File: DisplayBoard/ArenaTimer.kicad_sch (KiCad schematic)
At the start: 42 parts, among them J1 Blue ready-up, J10 Red ready-up, J12 Screw_Terminal_01x03, J13 WAGO, J14 WAGO, J15 Conn_01x15_Socket, J16 Conn_01x15_Socket, J2 Conn_01x02_Socket, J3 Conn_01x02_Pin, J4 GND, J5 5V, J6 GND, J7 5V, J8 PJ-082BH, J9 Conn_01x06_Pin, K1 G5V-2_Split, Q1 BSS214NW

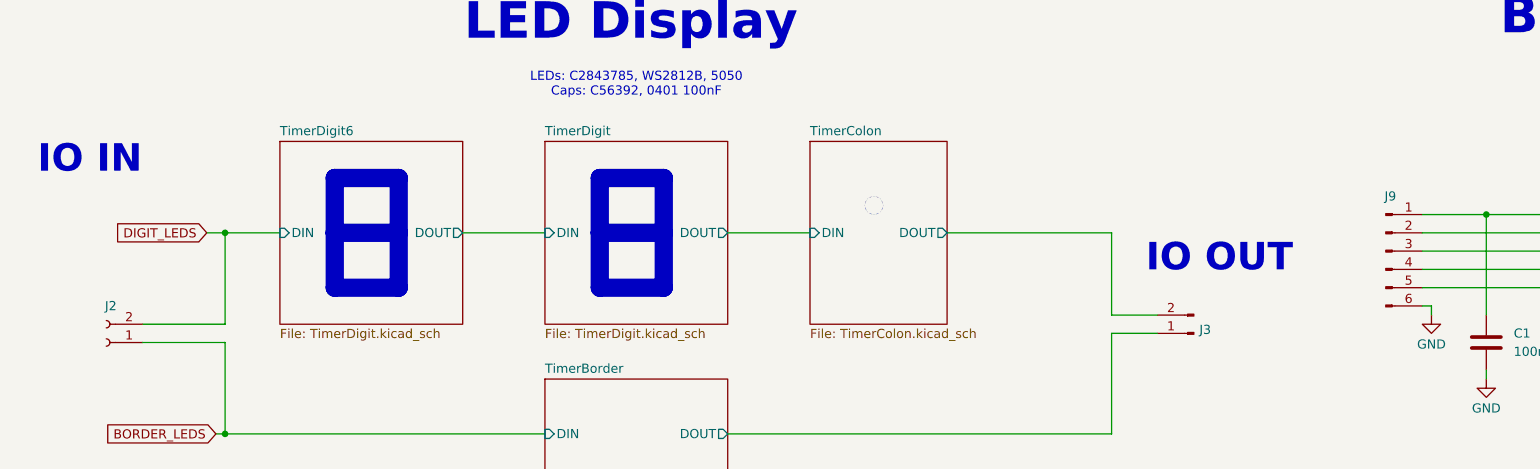
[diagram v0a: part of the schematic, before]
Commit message: flip BOUT/DOUT which is techncially flipped, but consistent with legacy HW.
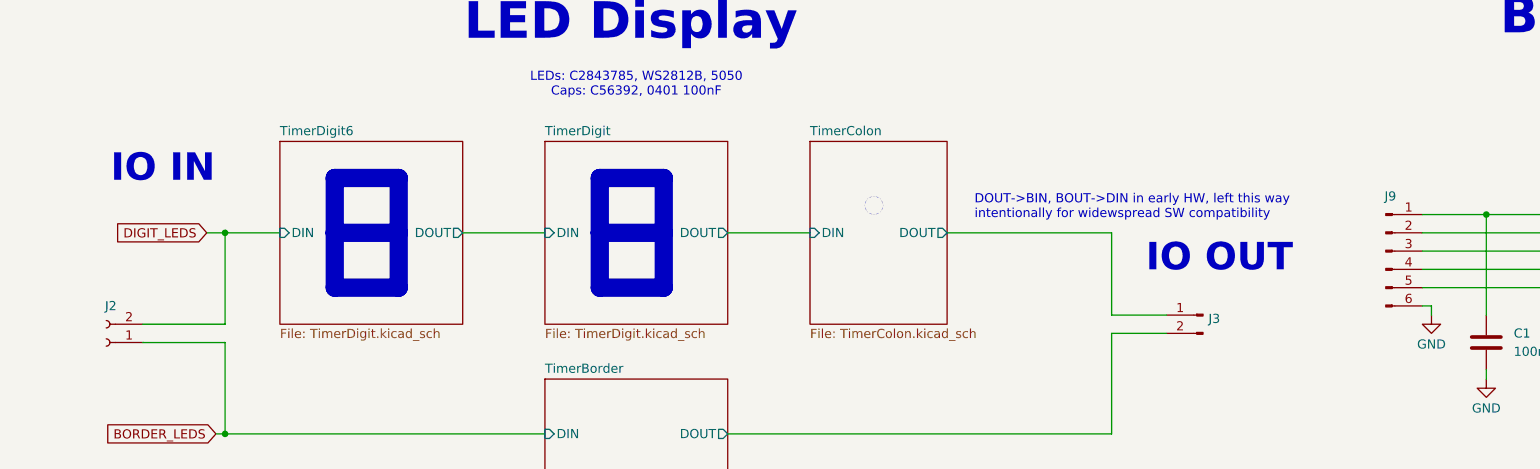
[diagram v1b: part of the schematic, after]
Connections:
- net TimerBorder/DOUT: now also J3.2 (Pin_2); no longer J3.1 (Pin_1)
- net TimerColon/DOUT: now also J3.1 (Pin_1); no longer J3.2 (Pin_2)
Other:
- note added: "DOUT->BIN, BOUT->DIN in early HW, left this way intentionally for widewspread SW compatibility"
- moved on the sheet: J3
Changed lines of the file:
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@@
 	(text "IO IN"
 		(exclude_from_sim no)
-		(at 28.194 50.8 0)
+		(at 38.354 52.07 0)
 		(effects
 			(font
@@
 		)
 	)
+	(text "DOUT->BIN, BOUT->DIN in early HW, left this way \nintentionally for widewspread SW compatibility"
+		(exclude_from_sim no)
+		(at 151.13 57.404 0)
+		(effects
+			(font
+				(size 1.27 1.27)
+			)
+			(justify left)
+		)
+	)
 	(text "LED Display"
 		(exclude_from_sim no)
@@
 	(wire
 		(pts
+			(xy 170.18 72.39) (xy 177.8 72.39)
+		)
+		(stroke
+			(width 0)
+			(type default)
+		)
+	)
+	(wire
+		(pts
 			(xy 309.88 200.66) (xy 309.88 203.2)
 		)
@@
 	(wire
 		(pts
-			(xy 170.18 72.39) (xy 176.53 72.39)
-		)
-		(stroke
-			(width 0)
-			(type default)
-		)
-	)
-	(wire
-		(pts
 			(xy 58.42 209.55) (xy 58.42 212.09)
 		)
@@
 	(wire
 		(pts
-			(xy 170.18 74.93) (xy 176.53 74.93)
-		)
-		(stroke
-			(width 0)
-			(type default)
-		)
-	)
-	(wire
-		(pts
 			(xy 69.85 140.97) (xy 86.36 140.97)
 		)
@@
 	(wire
 		(pts
+			(xy 170.18 74.93) (xy 177.8 74.93)
+		)
+		(stroke
+			(width 0)
+			(type default)
+		)
+	)
+	(wire
+		(pts
 			(xy 284.48 68.58) (xy 278.13 68.58)
 		)
@@
 	(symbol
 		(lib_id "Connector:Conn_01x02_Pin")
-		(at 181.61 74.93 180)
+		(at 182.88 72.39 0)
+		(mirror y)
 		(unit 1)
 		(body_style 1)
@@
 		(dnp no)
 		(property "Reference" "J3"
-			(at 182.372 74.422 0)
+			(at 183.642 72.898 0)
 			(show_name no)
 			(do_not_autoplace no)
@@
 		)
 		(property "Value" "Conn_01x02_Pin"
-			(at 182.88 74.9299 0)
+			(at 184.15 72.3901 0)
 			(hide yes)
 			(show_name no)
@@
 		)
 		(property "Footprint" "Connector_PinHeader_2.54mm:PinHeader_1x02_P2.54mm_Horizontal"
-			(at 181.61 74.93 0)
+			(at 182.88 72.39 0)
 			(hide yes)
 			(show_name no)
@@
 		)
 		(property "Datasheet" ""
-			(at 181.61 74.93 0)
+			(at 182.88 72.39 0)
 			(hide yes)
 			(show_name no)
@@
 		)
 		(property "Description" "Generic connector, single row, 01x02, script generated"
-			(at 181.61 74.93 0)
+			(at 182.88 72.39 0)
 			(hide yes)
 			(show_name no)
@@
 		)
 		(property "LCSC" "C492410"
-			(at 181.61 74.93 0)
+			(at 182.88 72.39 0)
 			(hide yes)
 			(show_name no)

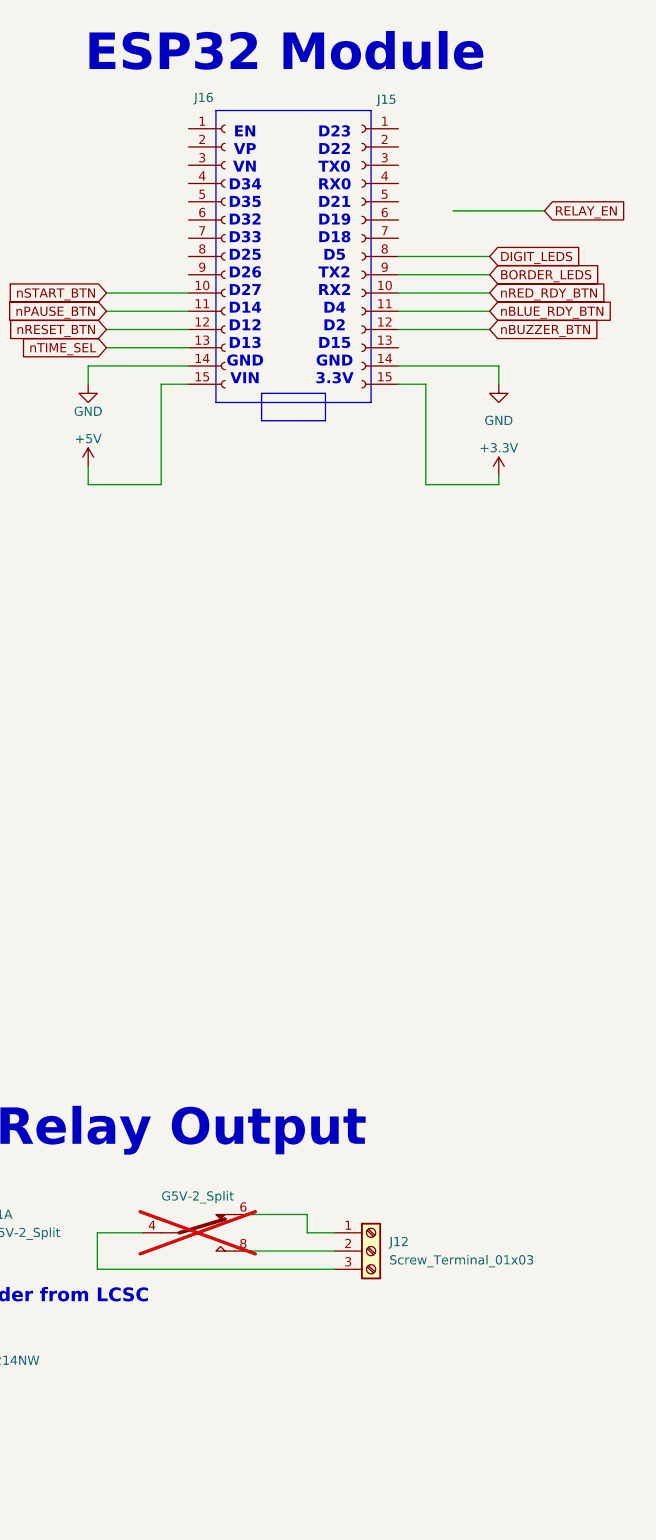
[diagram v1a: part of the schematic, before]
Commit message: clean up silk, resolve DRCs
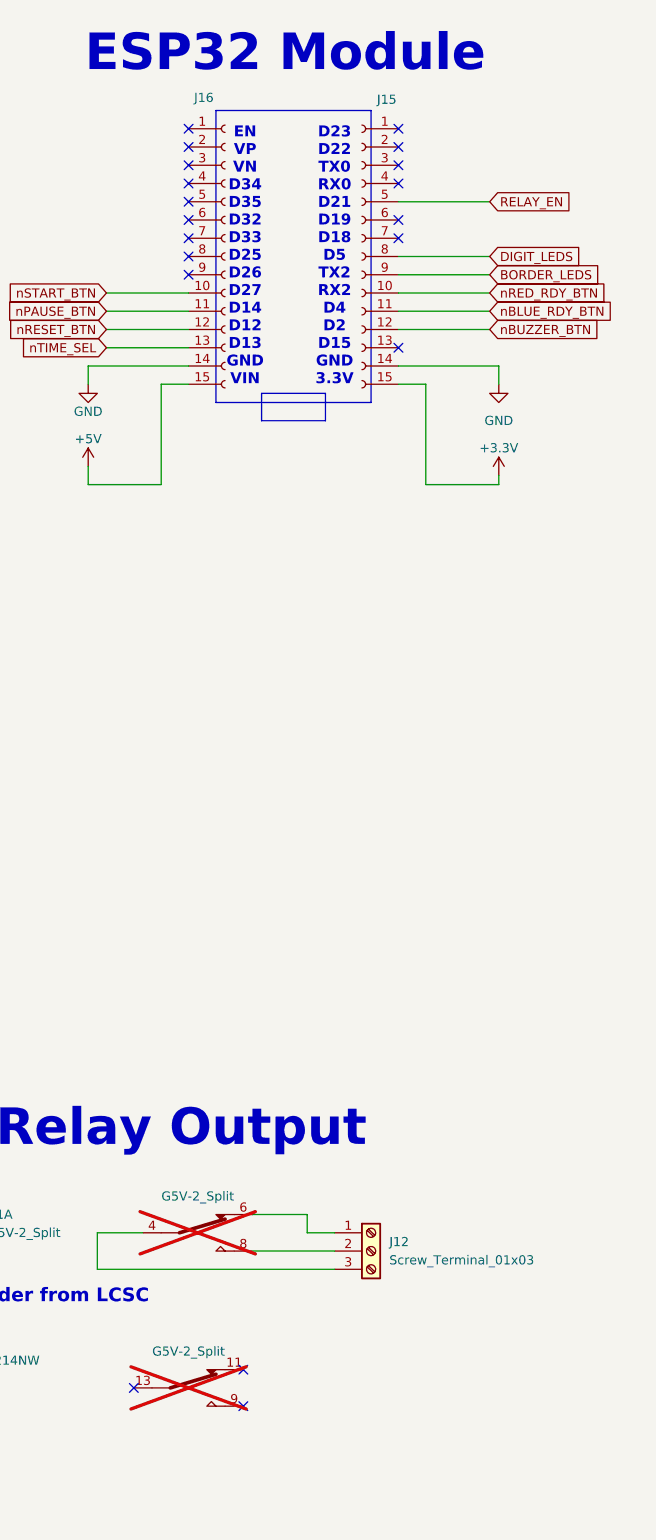
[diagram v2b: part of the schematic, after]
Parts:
- J12: footprint TerminalBlock:TerminalBlock_bornier-3_P5.08mm -> TerminalBlock:TerminalBlock_MaiXu_MX126-5.0-03P_1x03_P5.00mm
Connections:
- net RELAY_EN: now also J15.5 (Pin_5)
- no-connect marks 0 -> 19
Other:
- company: (none) -> SEMO Combat Robotics, Vinnie Marco
- title: (none) -> Arena Timer
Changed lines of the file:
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@@
 	(generator_version "10.0")
 	(paper "B")
+	(title_block
+		(title "Arena Timer")
+		(date "2026-05-26")
+		(rev "3")
+		(company "SEMO Combat Robotics, Vinnie Marco")
+	)
 	(rectangle
 		(start 347.98 35.56)
@@
 		(color 0 0 0 0)
 	)
+	(no_connect
+		(at 373.38 38.1)
+	)
+	(no_connect
+		(at 373.38 45.72)
+	)
+	(no_connect
+		(at 373.38 40.64)
+	)
+	(no_connect
+		(at 351.79 210.82)
+	)
+	(no_connect
+		(at 373.38 68.58)
+	)
+	(no_connect
+		(at 344.17 45.72)
+	)
+	(no_connect
+		(at 373.38 53.34)
+	)
+	(no_connect
+		(at 344.17 43.18)
+	)
+	(no_connect
+		(at 373.38 43.18)
+	)
+	(no_connect
+		(at 344.17 48.26)
+	)
+	(no_connect
+		(at 344.17 55.88)
+	)
+	(no_connect
+		(at 344.17 38.1)
+	)
+	(no_connect
+		(at 344.17 50.8)
+	)
+	(no_connect
+		(at 344.17 58.42)
+	)
+	(no_connect
+		(at 351.79 215.9)
+	)
+	(no_connect
+		(at 344.17 53.34)
+	)
+	(no_connect
+		(at 336.55 213.36)
+	)
+	(no_connect
+		(at 344.17 40.64)
+	)
+	(no_connect
+		(at 373.38 50.8)
+	)
 	(wire
 		(pts
@@
 	(wire
 		(pts
-			(xy 393.7 49.53) (xy 381 49.53)
+			(xy 386.08 48.26) (xy 373.38 48.26)
 		)
 		(stroke
@@
 	(global_label "RELAY_EN"
 		(shape input)
-		(at 393.7 49.53 0)
+		(at 386.08 48.26 0)
 		(fields_autoplaced yes)
 		(effects
@@
 		)
 		(property "Intersheetrefs" "${INTERSHEET_REFS}"
-			(at 405.7566 49.53 0)
+			(at 398.1366 48.26 0)
 			(hide yes)
 			(show_name no)
@@
 	)
 	(symbol
+		(lib_id "Relay:G5V-2_Split")
+		(at 344.17 213.36 270)
+		(unit 3)
+		(body_style 1)
+		(exclude_from_sim no)
+		(in_bom no)
+		(on_board yes)
+		(in_pos_files no)
+		(dnp yes)
+		(fields_autoplaced yes)
+		(property "Reference" "K1"
+			(at 344.17 205.74 90)
+			(hide yes)
+			(show_name no)
+			(do_not_autoplace no)
+			(effects
+				(font
+					(size 1.27 1.27)
+				)
+			)
+		)
+		(property "Value" "G5V-2_Split"
+			(at 344.17 208.28 90)
+			(show_name no)
+			(do_not_autoplace no)
+			(effects
+				(font
+					(size 1.27 1.27)
+				)
+			)
+		)
+		(property "Footprint" "Relay_THT:Relay_DPDT_Omron_G5V-2"
+			(at 340.36 219.71 0)
+			(hide yes)
+			(show_name no)
+			(do_not_autoplace no)
+			(effects
+				(font
+					(size 1.27 1.27)
+				)
+				(justify left)
+			)
+		)
+		(property "Datasheet" "http://omronfs.omron.com/en_US/ecb/products/pdf/en-g5v_2.pdf"
+			(at 344.17 213.36 0)
+			(hide yes)
+			(show_name no)
+			(do_not_autoplace no)
+			(effects
+				(font
+					(size 1.27 1.27)
+				)
+			)
+		)
+		(property "Description" "Relay Miniature Omron DPDT"
+			(at 344.17 213.36 0)
+			(hide yes)
+			(show_name no)
+			(do_not_autoplace no)
+			(effects
+				(font
+					(size 1.27 1.27)
+				)
+			)
+		)
+		(property "LCSC" "C27269"
+			(at 344.17 213.36 0)
+			(hide yes)
+			(show_name no)
+			(do_not_autoplace no)
+			(effects
+				(font
+					(size 1.27 1.27)
+				)
+			)
+		)
+		(pin "13"
+		)
+		(pin "8"
+		)
+		(pin "16"
+		)
+		(pin "11"
+		)
+		(pin "1"
+		)
+		(pin "4"
+		)
+		(pin "9"
+		)
+		(pin "6"
+		)
+		(instances
+			(project "ArenaTimer"
+				(path "/2260d661-eea4-49a1-9161-db3d613eeecd"
+					(reference "K1")
+					(unit 3)
+				)
+			)
+		)
+	)
+	(symbol
 		(lib_id "Device:R_US")
 		(at 294.64 213.36 0)
@@
 			)
 		)
-		(property "Footprint" "TerminalBlock:TerminalBlock_bornier-3_P5.08mm"
+		(property "Footprint" "TerminalBlock:TerminalBlock_MaiXu_MX126-5.0-03P_1x03_P5.00mm"
 			(at 369.57 194.31 0)
 			(hide yes)

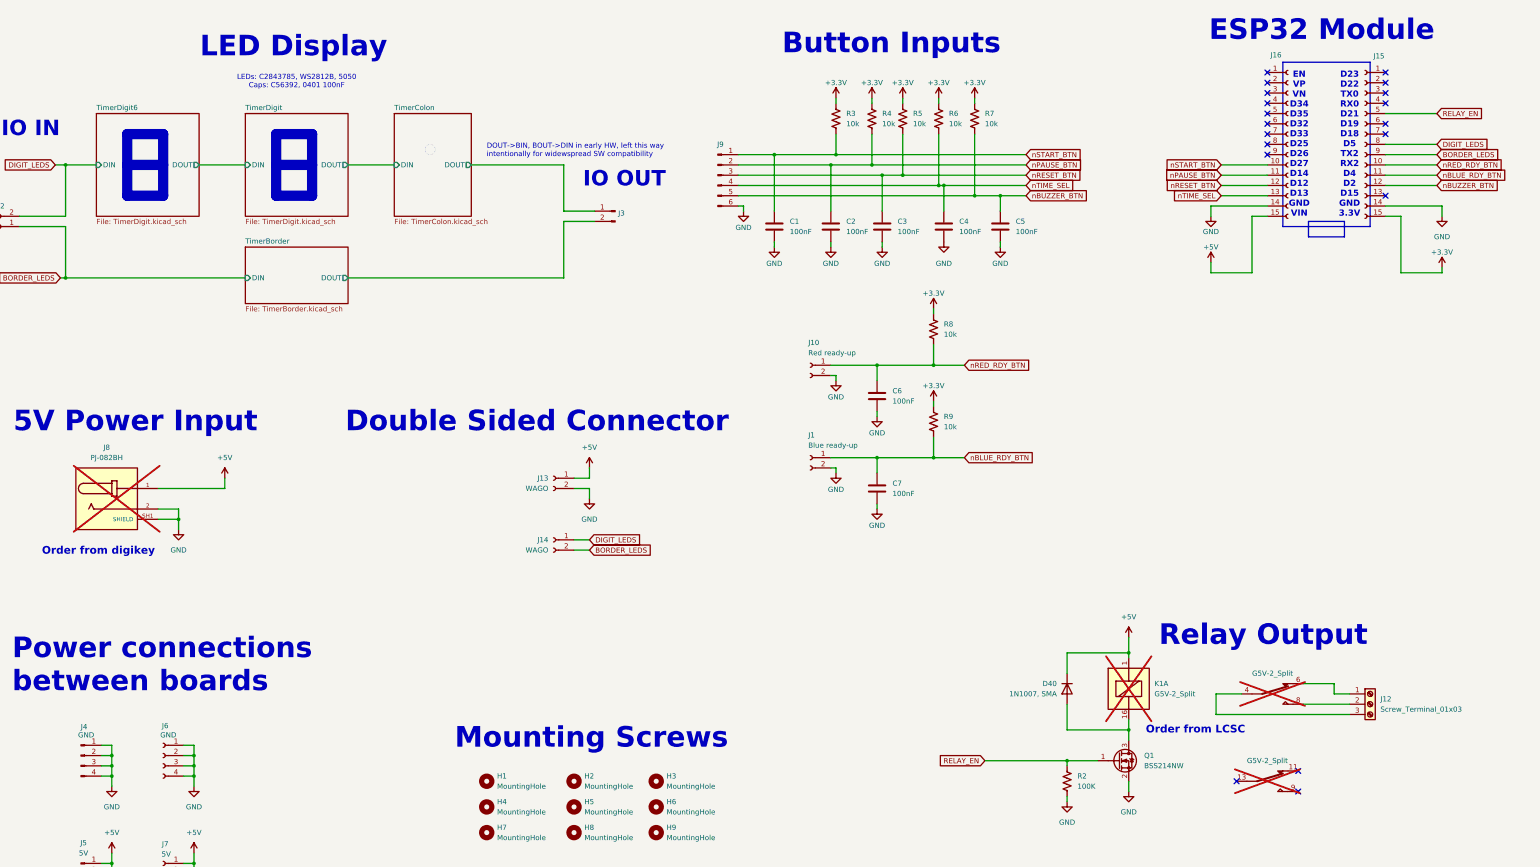
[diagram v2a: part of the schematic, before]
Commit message: more cleanup, added spare IO and power pads for expansion
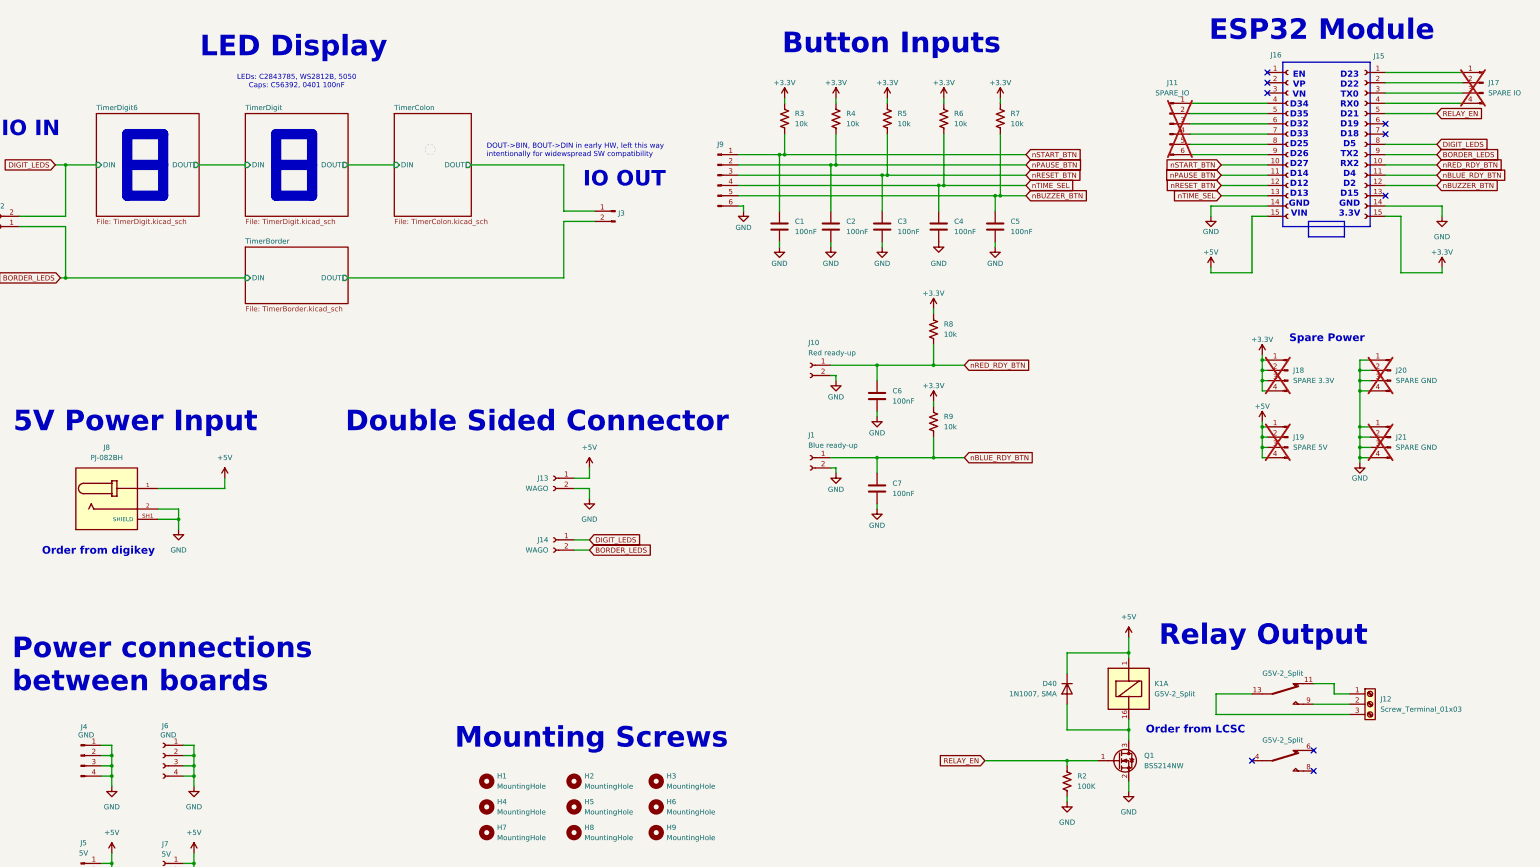
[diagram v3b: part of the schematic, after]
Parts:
- added J11: SPARE_IO, Connector_PinHeader_2.54mm:PinHeader_1x06_P2.54mm_Vertical, symbol Connector:Conn_01x06_Pin
- added J17: SPARE IO, Connector_PinHeader_2.54mm:PinHeader_1x04_P2.54mm_Vertical, symbol Connector:Conn_01x04_Pin
- added J18: SPARE 3.3V, Connector_PinHeader_2.54mm:PinHeader_1x04_P2.54mm_Vertical, symbol Connector:Conn_01x04_Pin
- added J19: SPARE 5V, Connector_PinHeader_2.54mm:PinHeader_1x04_P2.54mm_Vertical, symbol Connector:Conn_01x04_Pin
- added J20, J21: SPARE GND, Connector_PinHeader_2.54mm:PinHeader_1x04_P2.54mm_Vertical, symbol Connector:Conn_01x04_Pin
- added unit 3 of K1
- J8, K1: now fitted
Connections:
- net +3.3V: now also J18.1 (Pin_1), J18.2 (Pin_2), J18.3 (Pin_3), J18.4 (Pin_4)
- net +5V: now also J19.1 (Pin_1), J19.2 (Pin_2), J19.3 (Pin_3), J19.4 (Pin_4)
- net GND: now also J20.1 (Pin_1), J20.2 (Pin_2), J20.3 (Pin_3), J20.4 (Pin_4), J21.1 (Pin_1), J21.2 (Pin_2), J21.3 (Pin_3), J21.4 (Pin_4)
- net at K1.4: no longer J12.3 (Pin_3)
- net at K1.6: no longer J12.1 (Pin_1)
- net at K1.8: no longer J12.2 (Pin_2)
- net at J15.1 (Pin_1): now also J17.1 (Pin_1)
- net at J15.2 (Pin_2): now also J17.2 (Pin_2)
- net at J15.3 (Pin_3): now also J17.3 (Pin_3)
- net at J15.4 (Pin_4): now also J17.4 (Pin_4)
- net at J16.4 (Pin_4): now also J11.1 (Pin_1)
- net at J16.5 (Pin_5): now also J11.2 (Pin_2)
- net at J16.6 (Pin_6): now also J11.3 (Pin_3)
- net at J16.7 (Pin_7): now also J11.4 (Pin_4)
- net at J16.8 (Pin_8): now also J11.5 (Pin_5)
- net at J16.9 (Pin_9): now also J11.6 (Pin_6)
- new net: J12.1 (Pin_1), K1.11
- new net: J12.3 (Pin_3), K1.13
- new net: J12.2 (Pin_2), K1.9
- no-connect marks 19 -> 9
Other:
- note added: "Spare Power"
- moved on the sheet: C1, C4, C5, R3, R4, R5, R6, R7

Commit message: add beeper, generate production files
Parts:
- added BZ1: CEM-1203(42), Buzzer_Beeper:Buzzer_TDK_PS1240P02BT_D12.2mm_H6.5mm, symbol Device:Buzzer
- added D41: 1N4148WS, SOD323, Diode_SMD:D_SOD-323, symbol Device:D
- added Q2: BSS138, Package_TO_SOT_SMD:SOT-323_SC-70, symbol Transistor_FET:BSS214NW
- added R10: 100K, Resistor_SMD:R_0402_1005Metric, symbol Device:R_US
- C1, C2, C3, C4, C5, C6, C7: LCSC C14663 -> C1581
- J12: LCSC C72334 -> C8377; now left out of the parts list
- Q1: value BSS214NW -> BSS138; LCSC C412741 -> C5224267
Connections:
- net +5V: now also BZ1.1 (+), D41.1 (K)
- net GND: now also Q2.2 (S), R10.2
- net nBUZZER_BTN: now also J15.6 (Pin_6); no longer J15.12 (Pin_12)
- net nRESET_BTN: now also J15.13 (Pin_13); no longer J16.12 (Pin_12)
- net BEEPER_EN: now reaches J15.7 (Pin_7)
- net BEEPER_EN: now also Q2.1 (G), R10.1
- new net: BZ1.2 (-), D41.2 (A), Q2.3 (D)
- no-connect marks 9 -> 8
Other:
- note added: "Beeper"
- note added: "Mate with C71371"
- moved on the sheet: D40, H1, H2, H3, H4, H5, H6, H7, H8, H9, J12, J4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
